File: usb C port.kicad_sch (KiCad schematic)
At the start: 1 part, among them P1 USB4105-GF-A

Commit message: Schematic mostly finished
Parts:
- removed P1: USB4105-GF-A, symbol arisu-split:USB4105-GF-A
- added J6: USB4105-GF-A, arisu-split:USB4105-GF-A, symbol arisu-split:USB4105-GF-A
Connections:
- net +5V_L: now also J6.A4 (VBUS), J6.A9 (VBUS), J6.B4 (VBUS), J6.B9 (VBUS)
- net GND_L: now also J6.A1 (GND), J6.A12 (GND), J6.B1 (GND), J6.B12 (GND), J6.S1 (SHIELD)
- net USB_D+: now also J6.A6 (D+), J6.B6 (D+)
- net USB_D-: now also J6.A7 (D-), J6.B7 (D-)
- no-connect marks 2 -> 4
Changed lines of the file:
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@@
 (kicad_sch (version 20211123) (generator eeschema)
   (paper "A4")
-  (junction (at 82.55 92.71) (diameter 0) (color 0 0 0 0)
+  (junction (at 77.47 92.71) (diameter 0) (color 0 0 0 0)
   )
-  (junction (at 115.57 57.15) (diameter 0) (color 0 0 0 0)
-  )
-  (junction (at 74.93 92.71) (diameter 0) (color 0 0 0 0)
-  )
-  (no_connect (at 100.33 74.93))
   (no_connect (at 100.33 59.69))
-  (wire (pts (xy 115.57 57.15) (xy 115.57 77.47))
+  (no_connect (at 100.33 85.09))
+  (no_connect (at 100.33 82.55))
+  (no_connect (at 100.33 62.23))
+  (wire (pts (xy 100.33 72.39) (xy 100.33 74.93))
     (stroke (width 0) (type default) (color 0 0 0 0))
   )
-  (wire (pts (xy 74.93 92.71) (xy 82.55 92.71))
+  (wire (pts (xy 77.47 92.71) (xy 85.09 92.71))
     (stroke (width 0) (type default) (color 0 0 0 0))
   )
-  (wire (pts (xy 100.33 57.15) (xy 115.57 57.15))
+  (wire (pts (xy 100.33 67.31) (xy 100.33 69.85))
     (stroke (width 0) (type default) (color 0 0 0 0))
   )
-  (wire (pts (xy 74.93 93.98) (xy 74.93 92.71))
+  (wire (pts (xy 100.33 54.61) (xy 115.57 54.61))
     (stroke (width 0) (type default) (color 0 0 0 0))
   )
-  (wire (pts (xy 100.33 77.47) (xy 115.57 77.47))
-    (stroke (width 0) (type default) (color 0 0 0 0))
-  )
-  (wire (pts (xy 82.55 92.71) (xy 85.09 92.71))
+  (wire (pts (xy 77.47 93.98) (xy 77.47 92.71))
     (stroke (width 0) (type default) (color 0 0 0 0))
   )
@@
     (effects (font (size 1.27 1.27)) (justify left bottom))
   )
-  (hierarchical_label "USB_D-" (shape bidirectional) (at 100.33 69.85 0)
+  (hierarchical_label "USB_D-" (shape bidirectional) (at 100.33 67.31 0)
     (effects (font (size 1.27 1.27)) (justify left))
   )
-  (hierarchical_label "USB_D+" (shape bidirectional) (at 100.33 64.77 0)
+  (hierarchical_label "USB_D+" (shape bidirectional) (at 100.33 72.39 0)
     (effects (font (size 1.27 1.27)) (justify left))
   )
-  (symbol (lib_id "arisu-split:USB4105-GF-A") (at 82.55 69.85 0) (unit 1)
+  (symbol (lib_id "arisu-split:USB4105-GF-A") (at 85.09 69.85 0) (unit 1)
     (in_bom yes) (on_board yes) (fields_autoplaced)
-    (property "Reference" "P1" (id 0) (at 82.55 50.9102 0))
-    (property "Value" "USB4105-GF-A" (id 1) (at 82.55 53.4471 0))
-    (property "Footprint" "" (id 2) (at 86.36 67.31 0)
+    (property "Reference" "J6" (id 0) (at 85.09 48.3702 0))
+    (property "Value" "USB4105-GF-A" (id 1) (at 85.09 50.9071 0))
+    (property "Footprint" "arisu-split:USB4105-GF-A" (id 2) (at 88.9 69.85 0)
       (effects (font (size 1.27 1.27)) hide)
     )
-    (property "Datasheet" "" (id 3) (at 86.36 67.31 0)
+    (property "Datasheet" "https://www.usb.org/sites/default/files/documents/usb_type-c.zip" (id 3) (at 88.9 69.85 0)
       (effects (font (size 1.27 1.27)) hide)
     )
-    (pin "A1/B1")
-    (pin "A12/B12")
-    (pin "A4/B4")
-    (pin "A5/B5")
-    (pin "A6/B6")
-    (pin "A7/B7")
-    (pin "A8/B8")
-    (pin "A9/B9")
+    (pin "A1")
+    (pin "A12")
+    (pin "A4")
+    (pin "A5")
+    (pin "A6")
+    (pin "A7")
+    (pin "A8")
+    (pin "A9")
+    (pin "B1")
+    (pin "B12")
+    (pin "B4")
+    (pin "B5")
+    (pin "B6")
+    (pin "B7")
+    (pin "B8")
+    (pin "B9")
     (pin "S1")
   )
-  (symbol (lib_id "arisu-split:+5V_L") (at 115.57 57.15 0) (unit 1)
+  (symbol (lib_id "arisu-split:GND_L") (at 77.47 93.98 0) (unit 1)
     (in_bom yes) (on_board yes) (fields_autoplaced)
-    (property "Reference" "#PWR0133" (id 0) (at 115.57 60.96 0)
+    (property "Reference" "#PWR01" (id 0) (at 77.47 100.33 0)
       (effects (font (size 1.27 1.27)) hide)
     )
-    (property "Value" "+5V_L" (id 1) (at 115.57 53.5742 0))
-    (property "Footprint" "" (id 2) (at 115.57 57.15 0)
+    (property "Value" "GND_L" (id 1) (at 77.47 98.4234 0))
+    (property "Footprint" "" (id 2) (at 77.47 93.98 0)
       (effects (font (size 1.27 1.27)) hide)
     )
-    (property "Datasheet" "" (id 3) (at 115.57 57.15 0)
+    (property "Datasheet" "" (id 3) (at 77.47 93.98 0)
       (effects (font (size 1.27 1.27)) hide)
     )
     (pin "1")
   )
-  (symbol (lib_id "arisu-split:GND_L") (at 74.93 93.98 0) (unit 1)
+  (symbol (lib_id "arisu-split:+5V_L") (at 115.57 54.61 0) (unit 1)
     (in_bom yes) (on_board yes) (fields_autoplaced)
-    (property "Reference" "#PWR0136" (id 0) (at 74.93 100.33 0)
+    (property "Reference" "#PWR011" (id 0) (at 115.57 58.42 0)
       (effects (font (size 1.27 1.27)) hide)
     )
-    (property "Value" "GND_L" (id 1) (at 74.93 98.4234 0))
-    (property "Footprint" "" (id 2) (at 74.93 93.98 0)
+    (property "Value" "+5V_L" (id 1) (at 115.57 51.0342 0))
+    (property "Footprint" "" (id 2) (at 115.57 54.61 0)
       (effects (font (size 1.27 1.27)) hide)
     )
-    (property "Datasheet" "" (id 3) (at 74.93 93.98 0)
+    (property "Datasheet" "" (id 3) (at 115.57 54.61 0)
       (effects (font (size 1.27 1.27)) hide)
     )

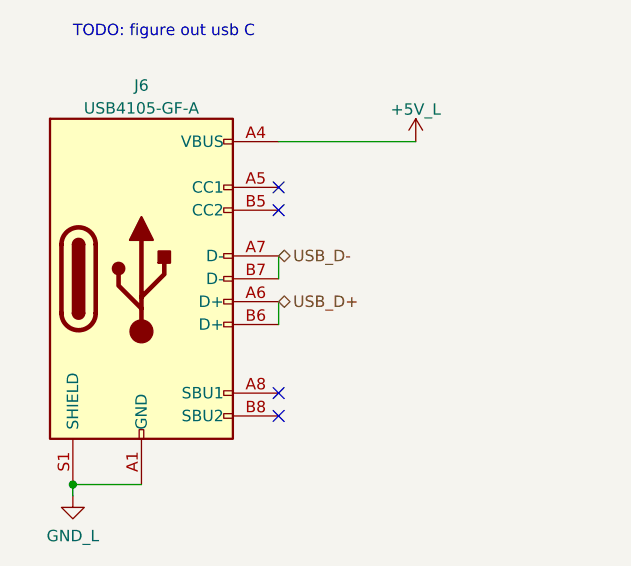
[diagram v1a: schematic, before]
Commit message: left side of keyboard finished for the time being
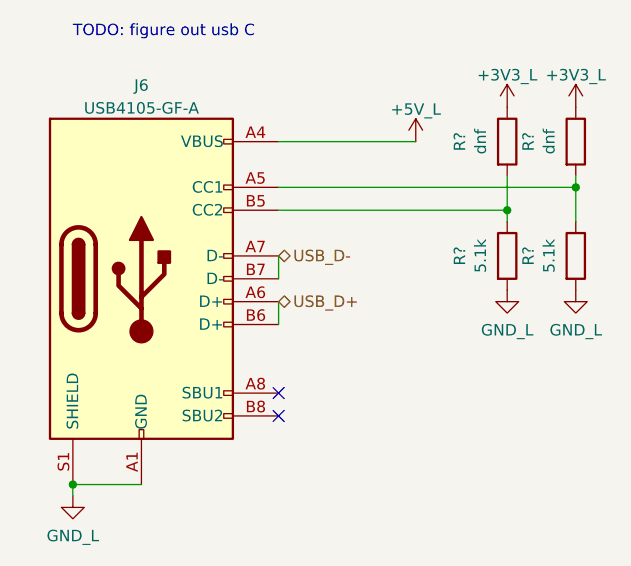
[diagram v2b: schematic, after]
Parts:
- added R? (x2): dnf, Capacitor_SMD:C_0603_1608Metric, symbol Device:R
- added R? (x2): 5.1k, Capacitor_SMD:C_0603_1608Metric, symbol Device:R
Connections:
- net GND_L: now also R?.2, R?.2
- net at J6.A5 (CC1): now also R?.1, R?.2
- net at J6.B5 (CC2): now also R?.1, R?.2
- new net +3V3_L: R?.1, R?.1
- no-connect marks 4 -> 2
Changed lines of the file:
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@@
 (kicad_sch (version 20211123) (generator eeschema)
   (paper "A4")
+  (junction (at 133.35 59.69) (diameter 0) (color 0 0 0 0)
+  )
+  (junction (at 125.73 62.23) (diameter 0) (color 0 0 0 0)
+  )
   (junction (at 77.47 92.71) (diameter 0) (color 0 0 0 0)
   )
-  (no_connect (at 100.33 59.69))
   (no_connect (at 100.33 85.09))
   (no_connect (at 100.33 82.55))
-  (no_connect (at 100.33 62.23))
   (wire (pts (xy 100.33 72.39) (xy 100.33 74.93))
     (stroke (width 0) (type default) (color 0 0 0 0))
   )
+  (wire (pts (xy 125.73 63.5) (xy 125.73 62.23))
+    (stroke (width 0) (type default) (color 0 0 0 0))
+  )
   (wire (pts (xy 77.47 92.71) (xy 85.09 92.71))
     (stroke (width 0) (type default) (color 0 0 0 0))
@@
     (stroke (width 0) (type default) (color 0 0 0 0))
   )
+  (wire (pts (xy 133.35 59.69) (xy 133.35 63.5))
+    (stroke (width 0) (type default) (color 0 0 0 0))
+  )
   (wire (pts (xy 100.33 54.61) (xy 115.57 54.61))
     (stroke (width 0) (type default) (color 0 0 0 0))
   )
+  (wire (pts (xy 133.35 58.42) (xy 133.35 59.69))
+    (stroke (width 0) (type default) (color 0 0 0 0))
+  )
+  (wire (pts (xy 125.73 58.42) (xy 125.73 62.23))
+    (stroke (width 0) (type default) (color 0 0 0 0))
+  )
+  (wire (pts (xy 100.33 62.23) (xy 125.73 62.23))
+    (stroke (width 0) (type default) (color 0 0 0 0))
+  )
   (wire (pts (xy 77.47 93.98) (xy 77.47 92.71))
+    (stroke (width 0) (type default) (color 0 0 0 0))
+  )
+  (wire (pts (xy 100.33 59.69) (xy 133.35 59.69))
     (stroke (width 0) (type default) (color 0 0 0 0))
   )
@@
   (hierarchical_label "USB_D+" (shape bidirectional) (at 100.33 72.39 0)
     (effects (font (size 1.27 1.27)) (justify left))
+  )
+  (symbol (lib_id "arisu-split:+3V3_L") (at 133.35 50.8 0) (unit 1)
+    (in_bom yes) (on_board yes) (fields_autoplaced)
+    (property "Reference" "#PWR?" (id 0) (at 133.35 54.61 0)
+      (effects (font (size 1.27 1.27)) hide)
+    )
+    (property "Value" "+3V3_L" (id 1) (at 133.35 47.2242 0))
+    (property "Footprint" "" (id 2) (at 133.35 50.8 0)
+      (effects (font (size 1.27 1.27)) hide)
+    )
+    (property "Datasheet" "" (id 3) (at 133.35 50.8 0)
+      (effects (font (size 1.27 1.27)) hide)
+    )
+    (pin "1")
   )
   (symbol (lib_id "arisu-split:USB4105-GF-A") (at 85.09 69.85 0) (unit 1)
@@
     (pin "S1")
   )
+  (symbol (lib_id "Device:R") (at 125.73 54.61 0) (unit 1)
+    (in_bom yes) (on_board yes)
+    (property "Reference" "R?" (id 0) (at 120.4722 54.61 90))
+    (property "Value" "dnf" (id 1) (at 122.7836 54.61 90))
+    (property "Footprint" "Capacitor_SMD:C_0603_1608Metric" (id 2) (at 123.952 54.61 90)
+      (effects (font (size 1.27 1.27)) hide)
+    )
+    (property "Datasheet" "~" (id 3) (at 125.73 54.61 0)
+      (effects (font (size 1.27 1.27)) hide)
+    )
+    (pin "1")
+    (pin "2")
+  )
   (symbol (lib_id "arisu-split:GND_L") (at 77.47 93.98 0) (unit 1)
     (in_bom yes) (on_board yes) (fields_autoplaced)
@@
     (pin "1")
   )
+  (symbol (lib_id "arisu-split:+3V3_L") (at 125.73 50.8 0) (unit 1)
+    (in_bom yes) (on_board yes) (fields_autoplaced)
+    (property "Reference" "#PWR?" (id 0) (at 125.73 54.61 0)
+      (effects (font (size 1.27 1.27)) hide)
+    )
+    (property "Value" "+3V3_L" (id 1) (at 125.73 47.2242 0))
+    (property "Footprint" "" (id 2) (at 125.73 50.8 0)
+      (effects (font (size 1.27 1.27)) hide)
+    )
+    (property "Datasheet" "" (id 3) (at 125.73 50.8 0)
+      (effects (font (size 1.27 1.27)) hide)
+    )
+    (pin "1")
+  )
+  (symbol (lib_id "arisu-split:GND_L") (at 133.35 71.12 0) (unit 1)
+    (in_bom yes) (on_board yes) (fields_autoplaced)
+    (property "Reference" "#PWR?" (id 0) (at 133.35 77.47 0)
+      (effects (font (size 1.27 1.27)) hide)
+    )
+    (property "Value" "GND_L" (id 1) (at 133.35 75.5634 0))
+    (property "Footprint" "" (id 2) (at 133.35 71.12 0)
+      (effects (font (size 1.27 1.27)) hide)
+    )
+    (property "Datasheet" "" (id 3) (at 133.35 71.12 0)
+      (effects (font (size 1.27 1.27)) hide)
+    )
+    (pin "1")
+  )
+  (symbol (lib_id "Device:R") (at 133.35 54.61 0) (unit 1)
+    (in_bom yes) (on_board yes)
+    (property "Reference" "R?" (id 0) (at 128.0922 54.61 90))
+    (property "Value" "dnf" (id 1) (at 130.4036 54.61 90))
+    (property "Footprint" "Capacitor_SMD:C_0603_1608Metric" (id 2) (at 131.572 54.61 90)
+      (effects (font (size 1.27 1.27)) hide)
+    )
+    (property "Datasheet" "~" (id 3) (at 133.35 54.61 0)
+      (effects (font (size 1.27 1.27)) hide)
+    )
+    (pin "1")
+    (pin "2")
+  )
   (symbol (lib_id "arisu-split:+5V_L") (at 115.57 54.61 0) (unit 1)
     (in_bom yes) (on_board yes) (fields_autoplaced)
@@
     (pin "1")
   )
+  (symbol (lib_id "arisu-split:GND_L") (at 125.73 71.12 0) (unit 1)
+    (in_bom yes) (on_board yes) (fields_autoplaced)
+    (property "Reference" "#PWR?" (id 0) (at 125.73 77.47 0)
+      (effects (font (size 1.27 1.27)) hide)
+    )
+    (property "Value" "GND_L" (id 1) (at 125.73 75.5634 0))
+    (property "Footprint" "" (id 2) (at 125.73 71.12 0)
+      (effects (font (size 1.27 1.27)) hide)
+    )
+    (property "Datasheet" "" (id 3) (at 125.73 71.12 0)
+      (effects (font (size 1.27 1.27)) hide)
+    )
+    (pin "1")
+  )
+  (symbol (lib_id "Device:R") (at 125.73 67.31 0) (unit 1)
+    (in_bom yes) (on_board yes)
+    (property "Reference" "R?" (id 0) (at 120.4722 67.31 90))
+    (property "Value" "5.1k" (id 1) (at 122.7836 67.31 90))
+    (property "Footprint" "Capacitor_SMD:C_0603_1608Metric" (id 2) (at 123.952 67.31 90)
+      (effects (font (size 1.27 1.27)) hide)
+    )
+    (property "Datasheet" "~" (id 3) (at 125.73 67.31 0)
+      (effects (font (size 1.27 1.27)) hide)
+    )
+    (pin "1")
+    (pin "2")
+  )
+  (symbol (lib_id "Device:R") (at 133.35 67.31 0) (unit 1)
+    (in_bom yes) (on_board yes)
+    (property "Reference" "R?" (id 0) (at 128.0922 67.31 90))
+    (property "Value" "5.1k" (id 1) (at 130.4036 67.31 90))
+    (property "Footprint" "Capacitor_SMD:C_0603_1608Metric" (id 2) (at 131.572 67.31 90)
+      (effects (font (size 1.27 1.27)) hide)
+    )
+    (property "Datasheet" "~" (id 3) (at 133.35 67.31 0)
+      (effects (font (size 1.27 1.27)) hide)
+    )
+    (pin "1")
+    (pin "2")
+  )
 )

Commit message: Left side case created in blender
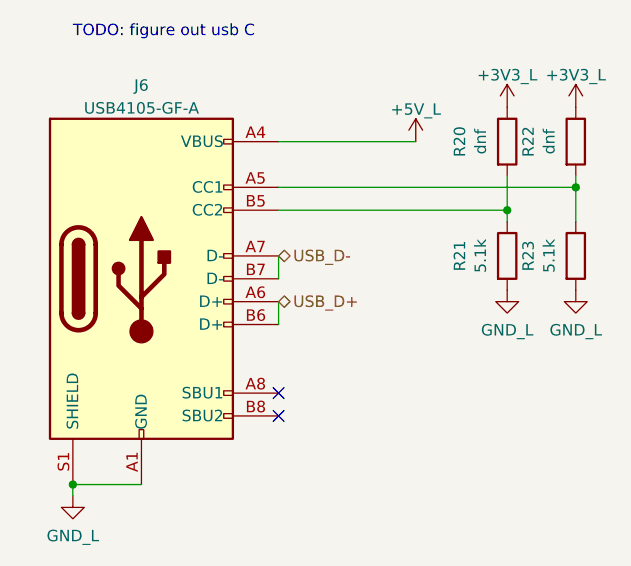
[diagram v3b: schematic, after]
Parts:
- gave numbers to parts that had none: 4
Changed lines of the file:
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@@
   (symbol (lib_id "arisu-split:+3V3_L") (at 133.35 50.8 0) (unit 1)
     (in_bom yes) (on_board yes) (fields_autoplaced)
-    (property "Reference" "#PWR?" (id 0) (at 133.35 54.61 0)
+    (property "Reference" "#PWR0164" (id 0) (at 133.35 54.61 0)
       (effects (font (size 1.27 1.27)) hide)
     )
@@
   (symbol (lib_id "Device:R") (at 125.73 54.61 0) (unit 1)
     (in_bom yes) (on_board yes)
-    (property "Reference" "R?" (id 0) (at 120.4722 54.61 90))
+    (property "Reference" "R20" (id 0) (at 120.4722 54.61 90))
     (property "Value" "dnf" (id 1) (at 122.7836 54.61 90))
     (property "Footprint" "Capacitor_SMD:C_0603_1608Metric" (id 2) (at 123.952 54.61 90)
@@
   (symbol (lib_id "arisu-split:+3V3_L") (at 125.73 50.8 0) (unit 1)
     (in_bom yes) (on_board yes) (fields_autoplaced)
-    (property "Reference" "#PWR?" (id 0) (at 125.73 54.61 0)
+    (property "Reference" "#PWR0163" (id 0) (at 125.73 54.61 0)
       (effects (font (size 1.27 1.27)) hide)
     )
@@
   (symbol (lib_id "arisu-split:GND_L") (at 133.35 71.12 0) (unit 1)
     (in_bom yes) (on_board yes) (fields_autoplaced)
-    (property "Reference" "#PWR?" (id 0) (at 133.35 77.47 0)
+    (property "Reference" "#PWR0161" (id 0) (at 133.35 77.47 0)
       (effects (font (size 1.27 1.27)) hide)
     )
@@
   (symbol (lib_id "Device:R") (at 133.35 54.61 0) (unit 1)
     (in_bom yes) (on_board yes)
-    (property "Reference" "R?" (id 0) (at 128.0922 54.61 90))
+    (property "Reference" "R22" (id 0) (at 128.0922 54.61 90))
     (property "Value" "dnf" (id 1) (at 130.4036 54.61 90))
     (property "Footprint" "Capacitor_SMD:C_0603_1608Metric" (id 2) (at 131.572 54.61 90)
@@
   (symbol (lib_id "arisu-split:GND_L") (at 125.73 71.12 0) (unit 1)
     (in_bom yes) (on_board yes) (fields_autoplaced)
-    (property "Reference" "#PWR?" (id 0) (at 125.73 77.47 0)
+    (property "Reference" "#PWR0162" (id 0) (at 125.73 77.47 0)
       (effects (font (size 1.27 1.27)) hide)
     )
@@
   (symbol (lib_id "Device:R") (at 125.73 67.31 0) (unit 1)
     (in_bom yes) (on_board yes)
-    (property "Reference" "R?" (id 0) (at 120.4722 67.31 90))
+    (property "Reference" "R21" (id 0) (at 120.4722 67.31 90))
     (property "Value" "5.1k" (id 1) (at 122.7836 67.31 90))
     (property "Footprint" "Capacitor_SMD:C_0603_1608Metric" (id 2) (at 123.952 67.31 90)
@@
   (symbol (lib_id "Device:R") (at 133.35 67.31 0) (unit 1)
     (in_bom yes) (on_board yes)
-    (property "Reference" "R?" (id 0) (at 128.0922 67.31 90))
+    (property "Reference" "R23" (id 0) (at 128.0922 67.31 90))
     (property "Value" "5.1k" (id 1) (at 130.4036 67.31 90))
     (property "Footprint" "Capacitor_SMD:C_0603_1608Metric" (id 2) (at 131.572 67.31 90)
